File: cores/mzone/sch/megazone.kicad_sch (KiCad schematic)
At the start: 8 parts

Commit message: mzone core
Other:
- sheet Shared RAM ports: added PXCK1; removed CLK1
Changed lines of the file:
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@@
 			)
 		)
-		(pin "CLK1" input
+		(pin "PXCK1" input
 			(at 138.43 201.93 180)
 			(effects

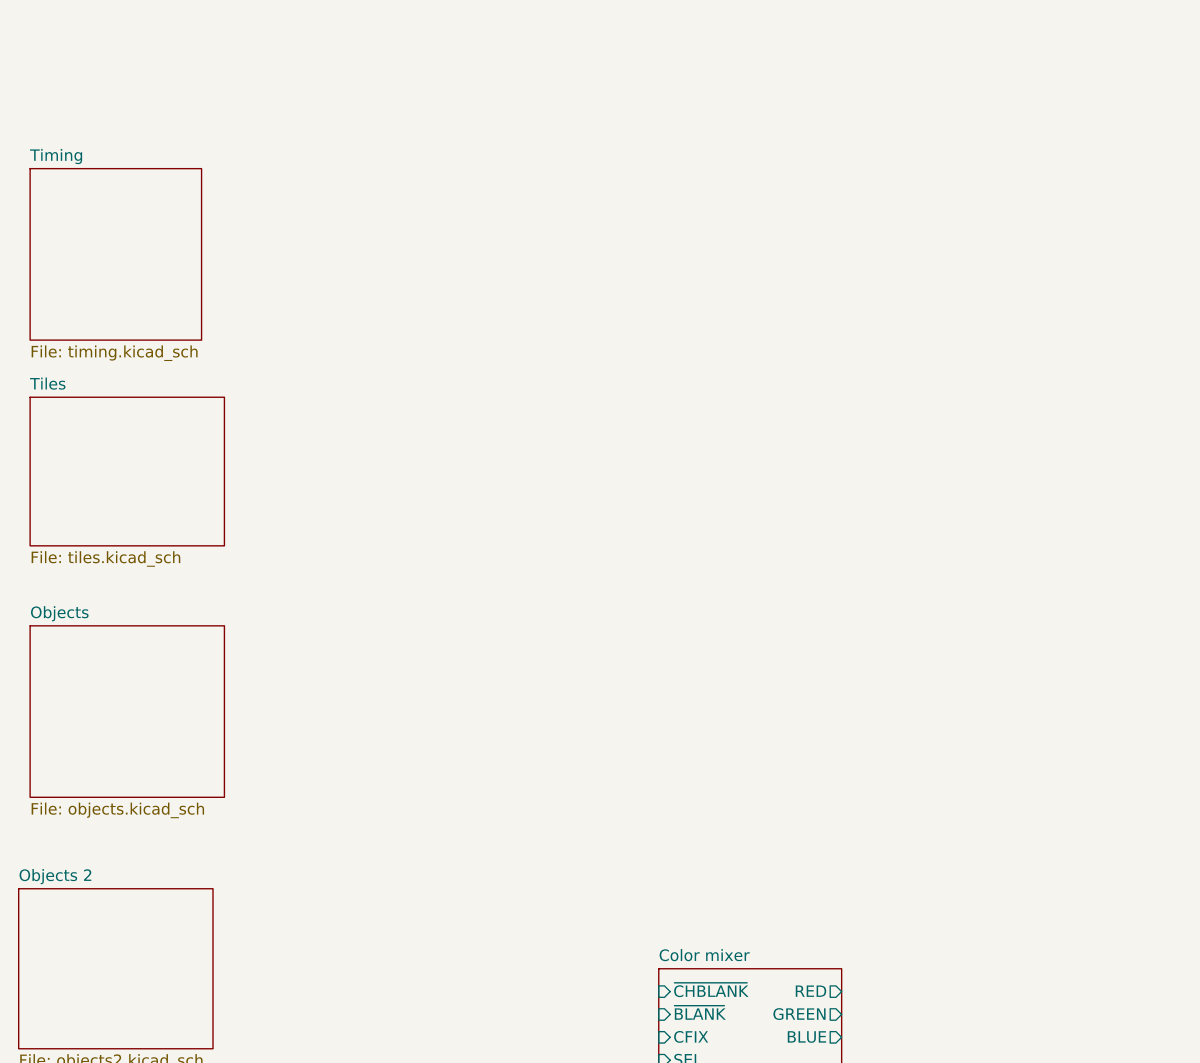
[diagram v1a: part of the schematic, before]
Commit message: mzone core
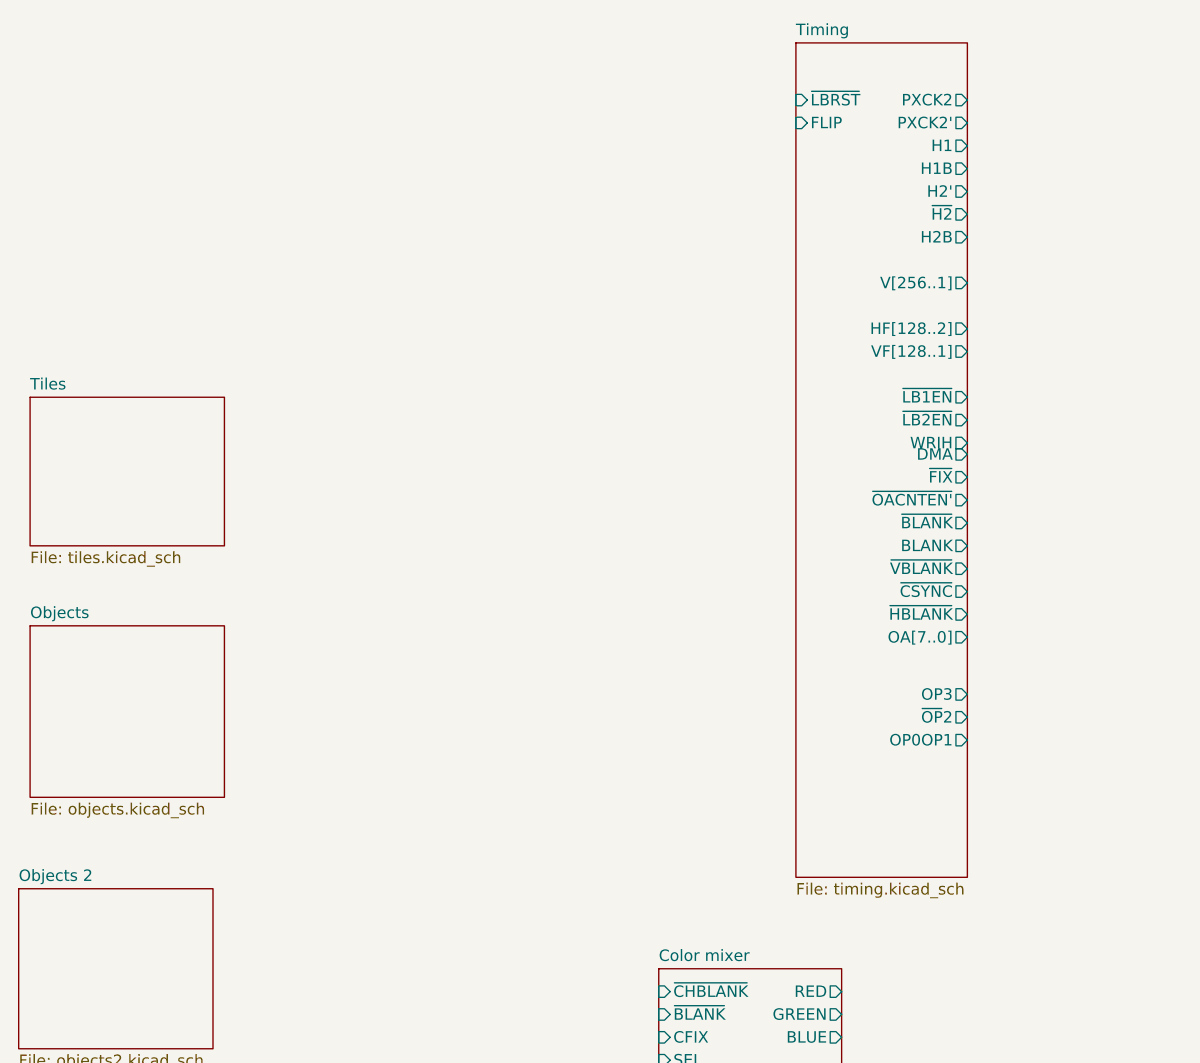
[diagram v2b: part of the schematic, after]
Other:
- sheet Timing ports: added BLANK, DMA, FLIP, H1, H1B, H2', H2B, HF[128..2], OA[7..0], OP0OP1, OP3, PXCK2, PXCK2', VF[128..1], V[256..1], WRIH, ~{BLANK}, ~{CSYNC}, ~{FIX}, ~{H2}, ~{HBLANK}, ~{LB1EN}, ~{LB2EN}, ~{LBRST}, ~{OACNTEN'}, ~{OP}2, ~{VBLANK}; removed none

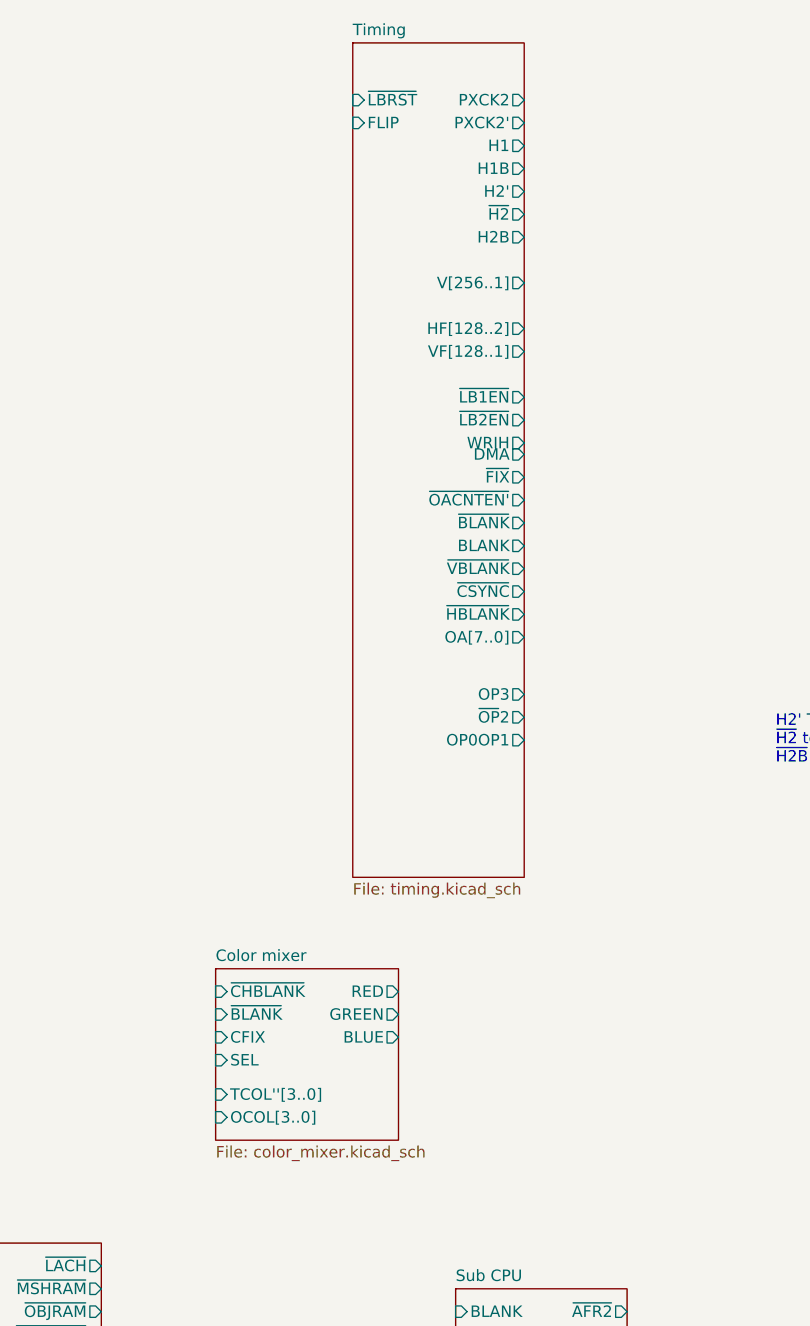
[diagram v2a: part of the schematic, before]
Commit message: mzone core
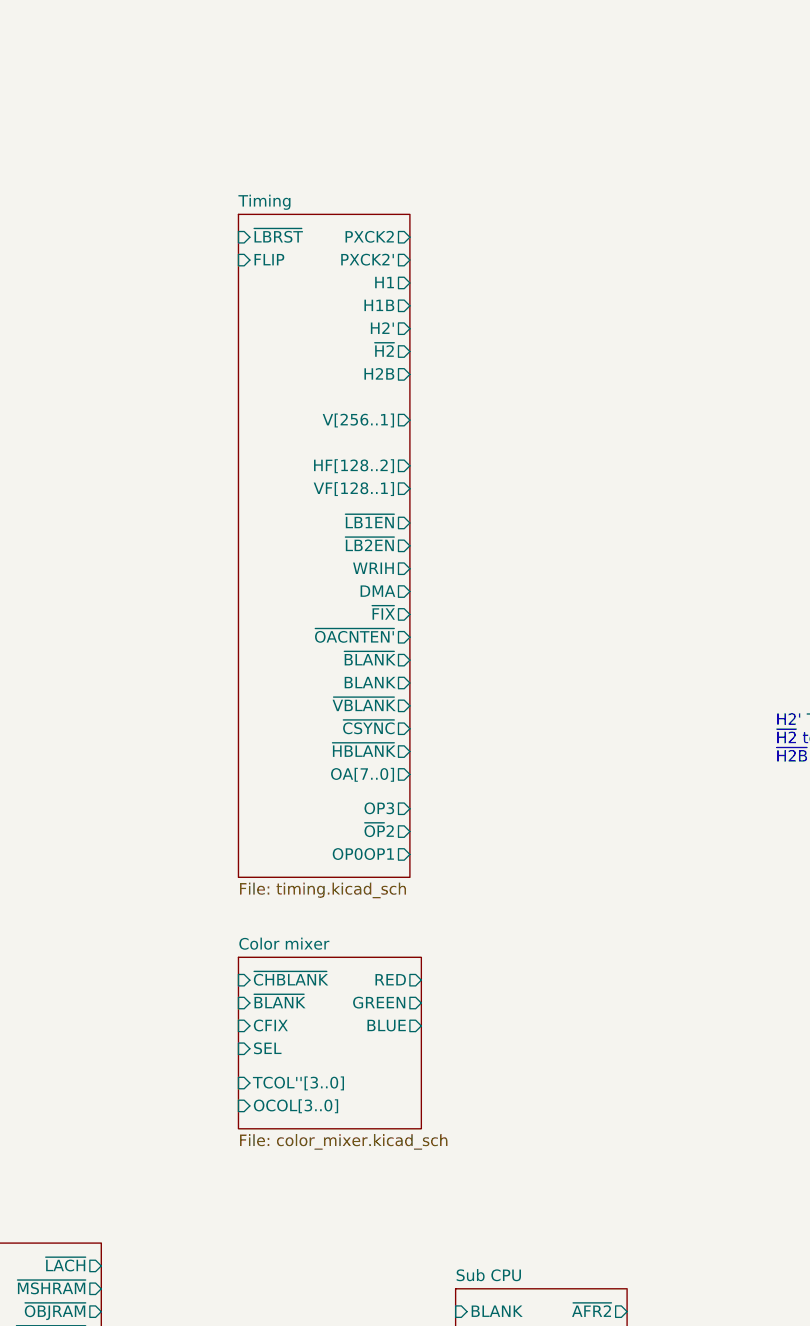
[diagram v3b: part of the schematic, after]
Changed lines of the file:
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@@
 	)
 	(sheet
-		(at 96.52 114.3)
+		(at 99.06 113.03)
 		(size 20.32 19.05)
 		(fields_autoplaced yes)
@@
 		)
 		(property "Sheetname" "Color mixer"
-			(at 96.52 113.5884 0)
+			(at 99.06 112.3184 0)
 			(effects
 				(font
@@
 		)
 		(property "Sheetfile" "color_mixer.kicad_sch"
-			(at 96.52 133.9346 0)
+			(at 99.06 132.6646 0)
 			(effects
 				(font
@@
 		)
 		(pin "OCOL[3..0]" input
-			(at 96.52 130.81 180)
+			(at 99.06 129.54 180)
 			(effects
 				(font
@@
 		)
 		(pin "TCOL''[3..0]" input
-			(at 96.52 128.27 180)
+			(at 99.06 127 180)
 			(effects
 				(font
@@
 		)
 		(pin "SEL" input
-			(at 96.52 124.46 180)
+			(at 99.06 123.19 180)
 			(effects
 				(font
@@
 		)
 		(pin "~{BLANK}" input
-			(at 96.52 119.38 180)
+			(at 99.06 118.11 180)
 			(effects
 				(font
@@
 		)
 		(pin "CFIX" input
-			(at 96.52 121.92 180)
+			(at 99.06 120.65 180)
 			(effects
 				(font
@@
 		)
 		(pin "~{CHBLANK}" input
-			(at 96.52 116.84 180)
+			(at 99.06 115.57 180)
 			(effects
 				(font
@@
 		)
 		(pin "RED" output
-			(at 116.84 116.84 0)
+			(at 119.38 115.57 0)
 			(effects
 				(font
@@
 		)
 		(pin "GREEN" output
-			(at 116.84 119.38 0)
+			(at 119.38 118.11 0)
 			(effects
 				(font
@@
 		)
 		(pin "BLUE" output
-			(at 116.84 121.92 0)
+			(at 119.38 120.65 0)
 			(effects
 				(font
@@
 	)
 	(sheet
-		(at 111.76 11.43)
-		(size 19.05 92.71)
+		(at 99.06 30.48)
+		(size 19.05 73.66)
 		(fields_autoplaced yes)
 		(stroke
@@
 		)
 		(property "Sheetname" "Timing"
-			(at 111.76 10.7184 0)
+			(at 99.06 29.7684 0)
 			(effects
 				(font
@@
 		)
 		(property "Sheetfile" "timing.kicad_sch"
-			(at 111.76 104.7246 0)
+			(at 99.06 104.7246 0)
 			(effects
 				(font
@@
 		)
 		(pin "OA[7..0]" output
-			(at 130.81 77.47 0)
+			(at 118.11 92.71 0)
 			(effects
 				(font
@@
 		)
 		(pin "~{BLANK}" output
-			(at 130.81 64.77 0)
+			(at 118.11 80.01 0)
 			(effects
 				(font
@@
 		)
 		(pin "~{OACNTEN'}" output
-			(at 130.81 62.23 0)
+			(at 118.11 77.47 0)
 			(effects
 				(font
@@
 		)
 		(pin "BLANK" output
-			(at 130.81 67.31 0)
+			(at 118.11 82.55 0)
 			(effects
 				(font
@@
 		)
 		(pin "~{VBLANK}" output
-			(at 130.81 69.85 0)
+			(at 118.11 85.09 0)
 			(effects
 				(font
@@
 		)
 		(pin "~{LBRST}" input
-			(at 111.76 17.78 180)
+			(at 99.06 33.02 180)
 			(effects
 				(font
@@
 		)
 		(pin "DMA" output
-			(at 130.81 57.15 0)
+			(at 118.11 72.39 0)
 			(effects
 				(font
@@
 		)
 		(pin "WRIH" output
-			(at 130.81 55.88 0)
+			(at 118.11 69.85 0)
 			(effects
 				(font
@@
 		)
 		(pin "~{LB2EN}" output
-			(at 130.81 53.34 0)
+			(at 118.11 67.31 0)
 			(effects
 				(font
@@
 		)
 		(pin "~{LB1EN}" output
-			(at 130.81 50.8 0)
+			(at 118.11 64.77 0)
 			(effects
 				(font
@@
 		)
 		(pin "H1B" output
-			(at 130.81 25.4 0)
+			(at 118.11 40.64 0)
 			(effects
 				(font
@@
 		)
 		(pin "HF[128..2]" output
-			(at 130.81 43.18 0)
+			(at 118.11 58.42 0)
 			(effects
 				(font
@@
 		)
 		(pin "~{CSYNC}" output
-			(at 130.81 72.39 0)
+			(at 118.11 87.63 0)
 			(effects
 				(font
@@
 		)
 		(pin "VF[128..1]" output
-			(at 130.81 45.72 0)
+			(at 118.11 60.96 0)
 			(effects
 				(font
@@
 		)
 		(pin "V[256..1]" output
-			(at 130.81 38.1 0)
+			(at 118.11 53.34 0)
 			(effects
 				(font
@@
 		)
 		(pin "OP3" output
-			(at 130.81 83.82 0)
+			(at 118.11 96.52 0)
 			(effects
 				(font
@@
 		)
 		(pin "~{OP}2" output
-			(at 130.81 86.36 0)
+			(at 118.11 99.06 0)
 			(effects
 				(font
@@
 		)
 		(pin "H1" output
-			(at 130.81 22.86 0)
+			(at 118.11 38.1 0)
 			(effects
 				(font
@@
 		)
 		(pin "FLIP" input
-			(at 111.76 20.32 180)
+			(at 99.06 35.56 180)
 			(effects
 				(font
@@
 		)
 		(pin "OP0OP1" output
-			(at 130.81 88.9 0)
+			(at 118.11 101.6 0)
 			(effects
 				(font
@@
 		)
 		(pin "PXCK2" output
-			(at 130.81 17.78 0)
+			(at 118.11 33.02 0)
 			(effects
 				(font
@@
 		)
 		(pin "PXCK2'" output
-			(at 130.81 20.32 0)
+			(at 118.11 35.56 0)
 			(effects
 				(font
@@
 		)
 		(pin "~{FIX}" output
-			(at 130.81 59.69 0)
+			(at 118.11 74.93 0)
 			(effects
 				(font
@@
 		)
 		(pin "~{HBLANK}" output
-			(at 130.81 74.93 0)
+			(at 118.11 90.17 0)
 			(effects
 				(font
@@
 		)
 		(pin "H2'" output
-			(at 130.81 27.94 0)
+			(at 118.11 43.18 0)
 			(effects
 				(font
@@
 		)
 		(pin "~{H2}" output
-			(at 130.81 30.48 0)
+			(at 118.11 45.72 0)
 			(effects
 				(font
@@
 		)
 		(pin "H2B" output
-			(at 130.81 33.02 0)
-			(effects
-				(font
+			(at 118.11 48.26 0)
+			(effects
+				(font

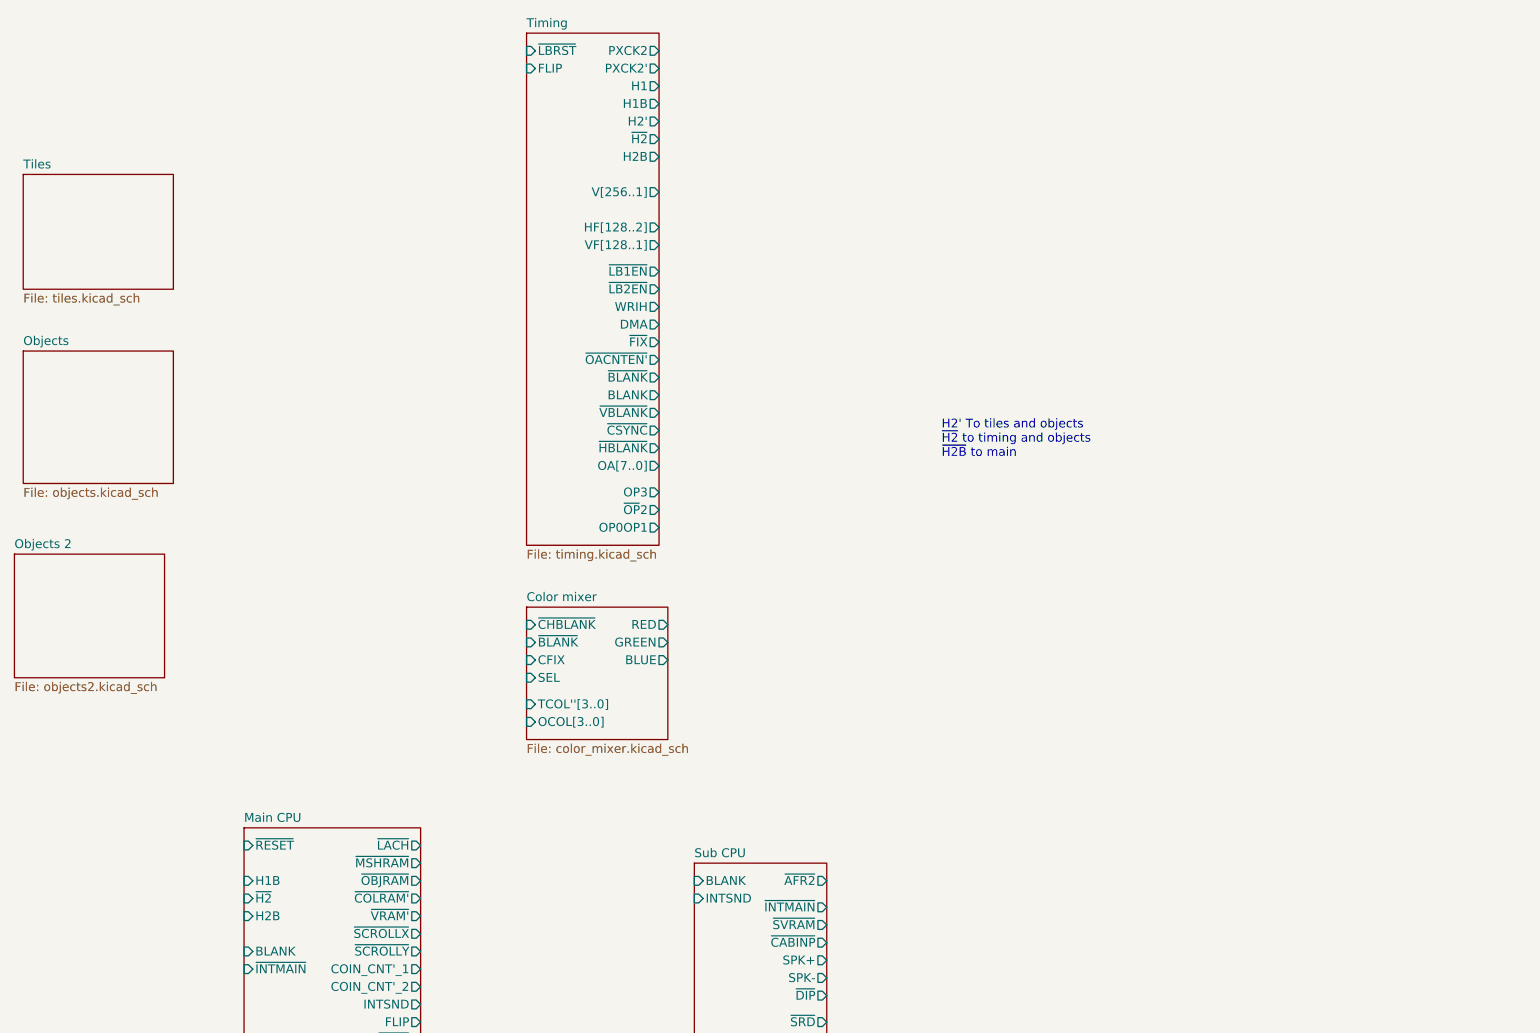
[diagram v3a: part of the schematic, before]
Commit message: mzone core
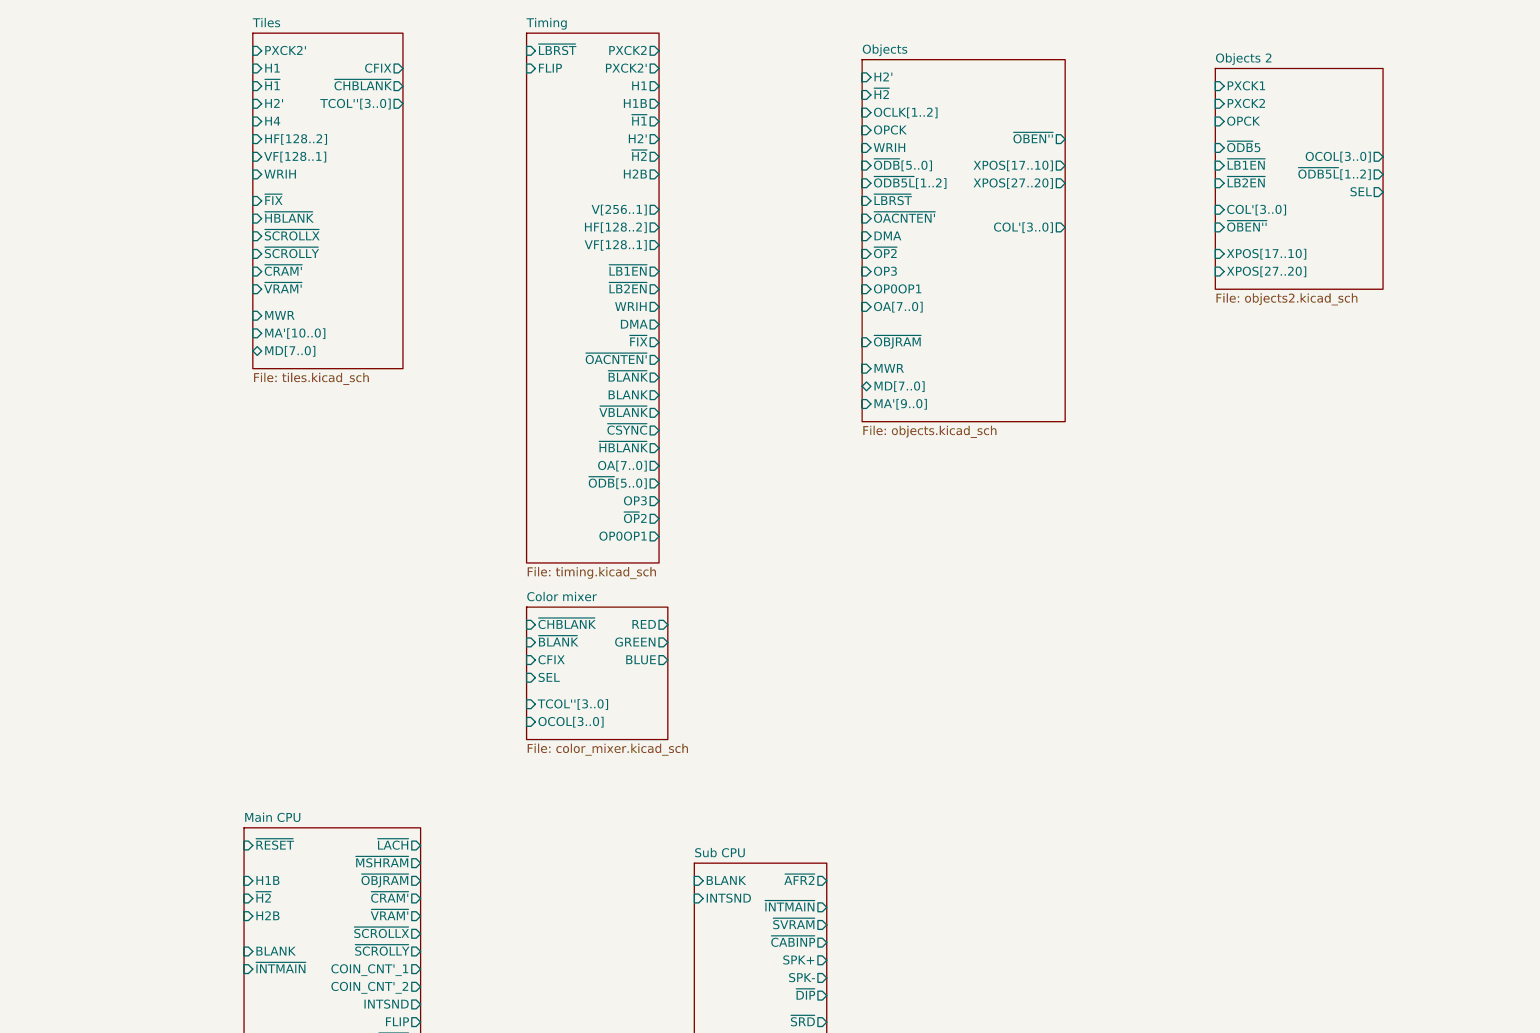
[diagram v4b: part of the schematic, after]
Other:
- sheet Main CPU ports: added ~{CRAM'}; removed ~{COLRAM'}
- sheet Objects ports: added COL'[3..0], DMA, H2', MA'[9..0], MD[7..0], MWR, OA[7..0], OCLK[1..2], OP0OP1, OP3, OPCK, WRIH, XPOS[17..10], XPOS[27..20], ~{H2}, ~{LBRST}, ~{OACNTEN'}, ~{OBEN''}, ~{OBJRAM}, ~{ODB5L}[1..2], ~{ODB}[5..0], ~{OP2}; removed none
- sheet Objects 2 ports: added COL'[3..0], OCOL[3..0], OPCK, PXCK1, PXCK2, SEL, XPOS[17..10], XPOS[27..20], ~{LB1EN}, ~{LB2EN}, ~{OBEN''}, ~{ODB5L}[1..2], ~{ODB}5; removed none
- sheet Tiles ports: added CFIX, H1, H2', H4, HF[128..2], MA'[10..0], MD[7..0], MWR, PXCK2', TCOL''[3..0], VF[128..1], WRIH, ~{CHBLANK}, ~{CRAM'}, ~{FIX}, ~{H1}, ~{HBLANK}, ~{SCROLLX}, ~{SCROLLY}, ~{VRAM'}; removed none
- sheet Timing ports: added ~{H1}, ~{ODB}[5..0]; removed none
- note removed: "H2' To tiles and objects ~{H2} to timing and objects ~{H2B} to main"
